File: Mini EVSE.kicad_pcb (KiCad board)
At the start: 2 copper layers, 49.5 x 76.8 mm, 46 parts, among them IC1 ATtiny84-20P, IC2 UCC23511QDWYRQ1, IC3 TLP3547_TP1,F_O, IC4 ISO224ADWV, J1 ICP, SW1 SW_DIP_x01, X1 15.36MHz

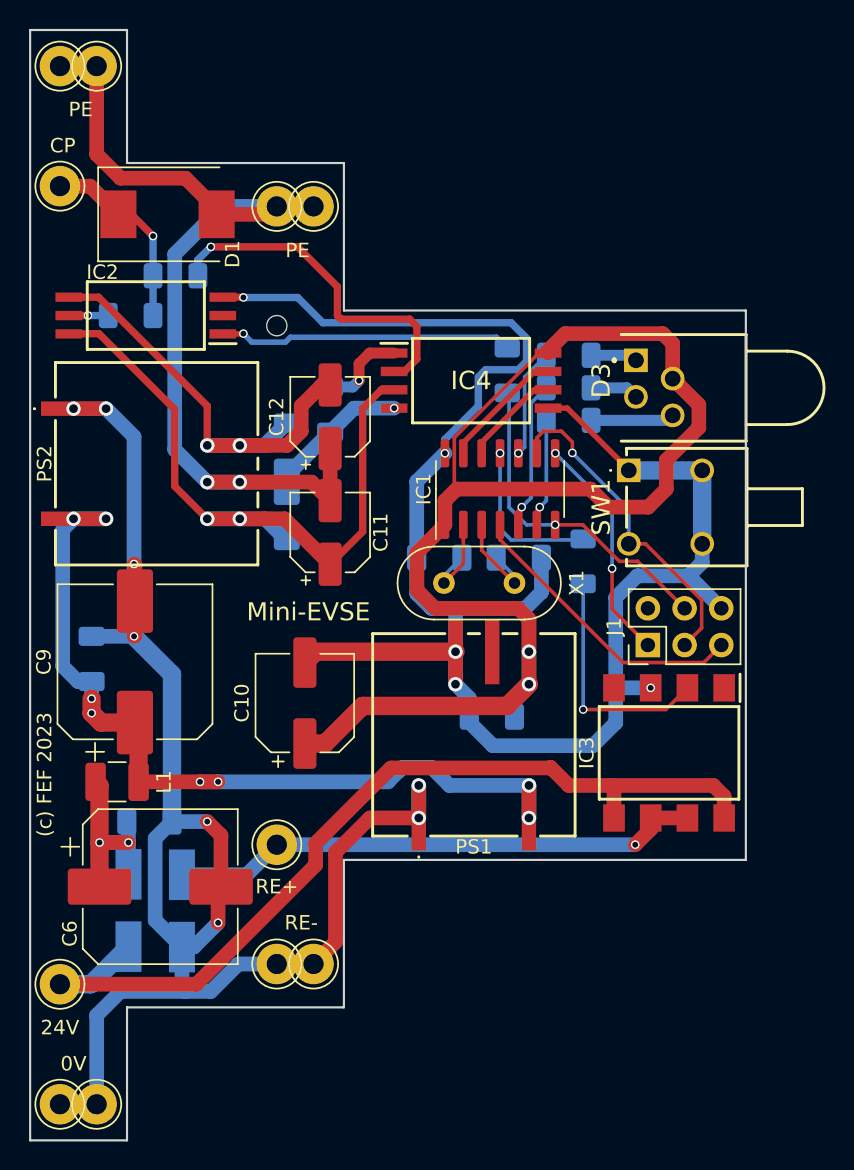
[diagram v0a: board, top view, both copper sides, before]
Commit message: More decoupling, layout adjustments
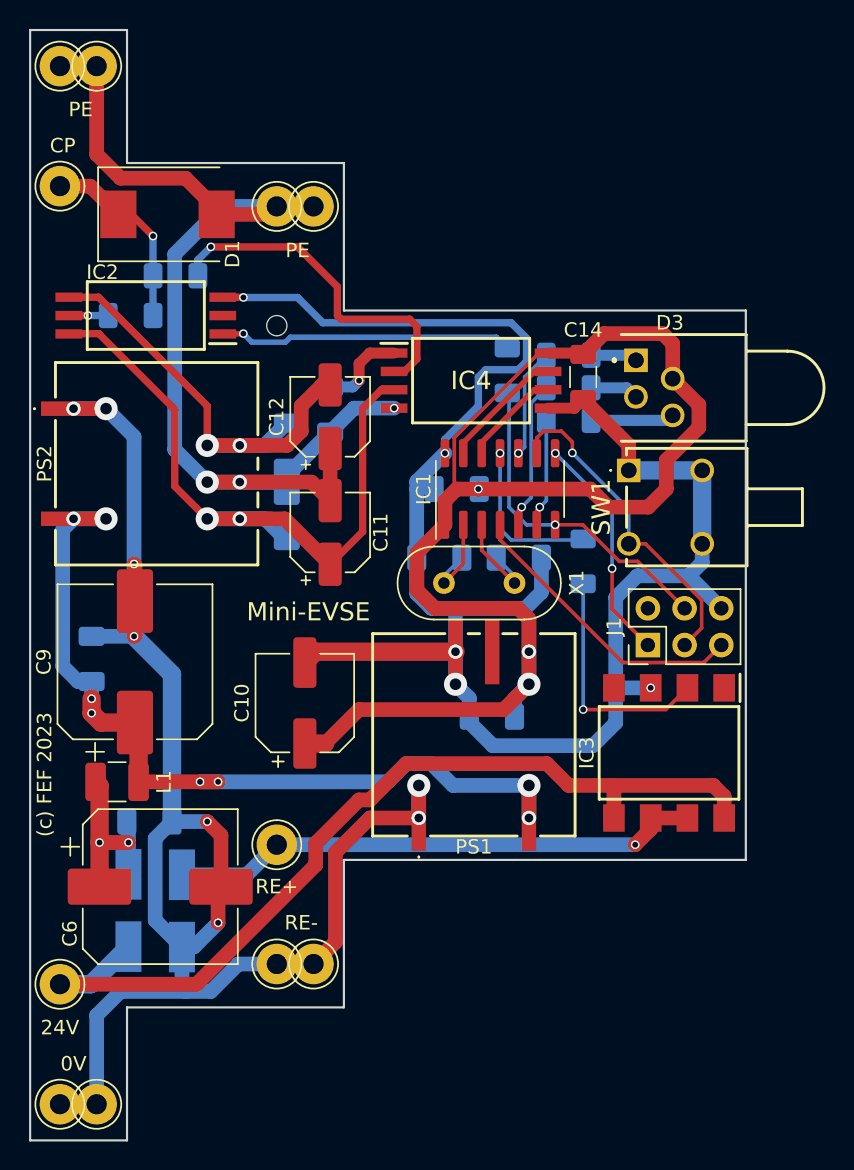
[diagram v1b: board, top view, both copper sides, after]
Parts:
- added C14: 10n, Capacitor_SMD:C_1206_3216Metric_Pad1.33x1.80mm_HandSolder, F.Cu at (138.2, 74.0)
- added C15: 10n, Capacitor_SMD:C_1206_3216Metric_Pad1.33x1.80mm_HandSolder, B.Cu at (129.5, 81.8)
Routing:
- net GND: track 126.8 -> 129.5 mm
- net +5V: track 90.4 -> 90.5 mm, vias 2 -> 3

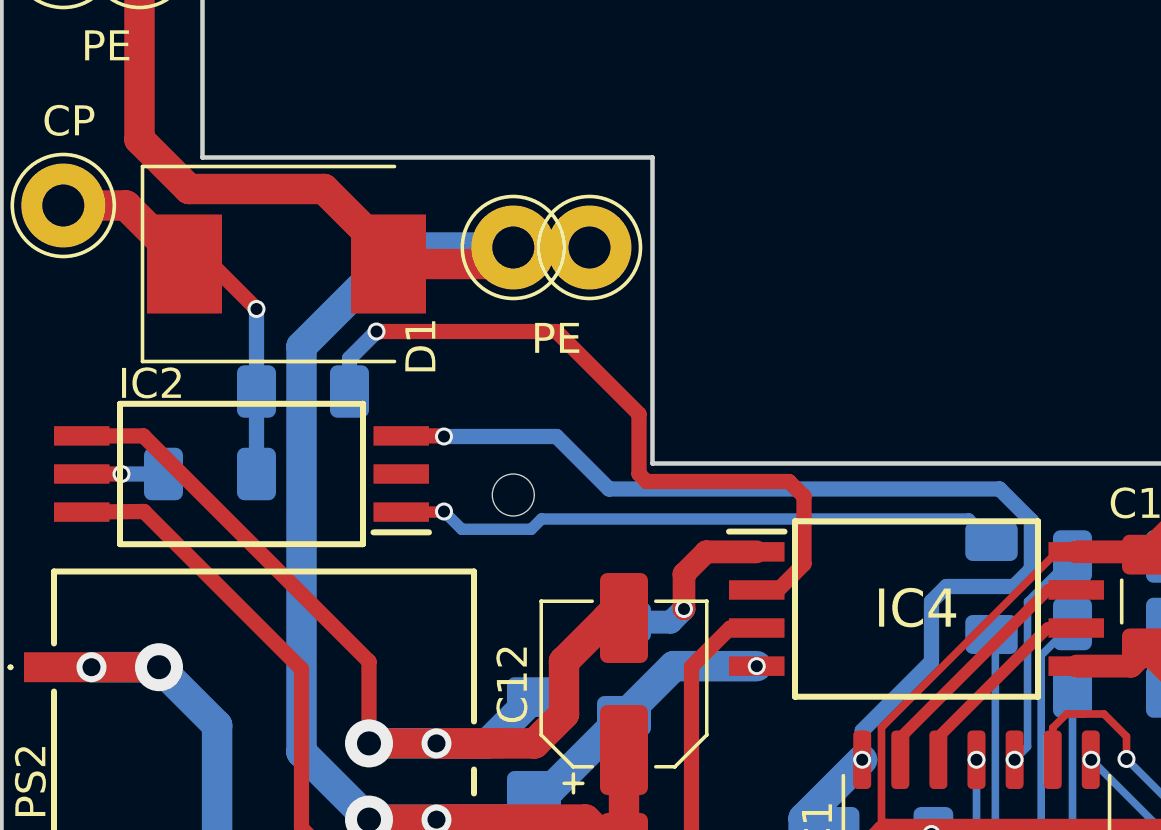
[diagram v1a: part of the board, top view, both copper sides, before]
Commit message: Added possible input decoupling cap
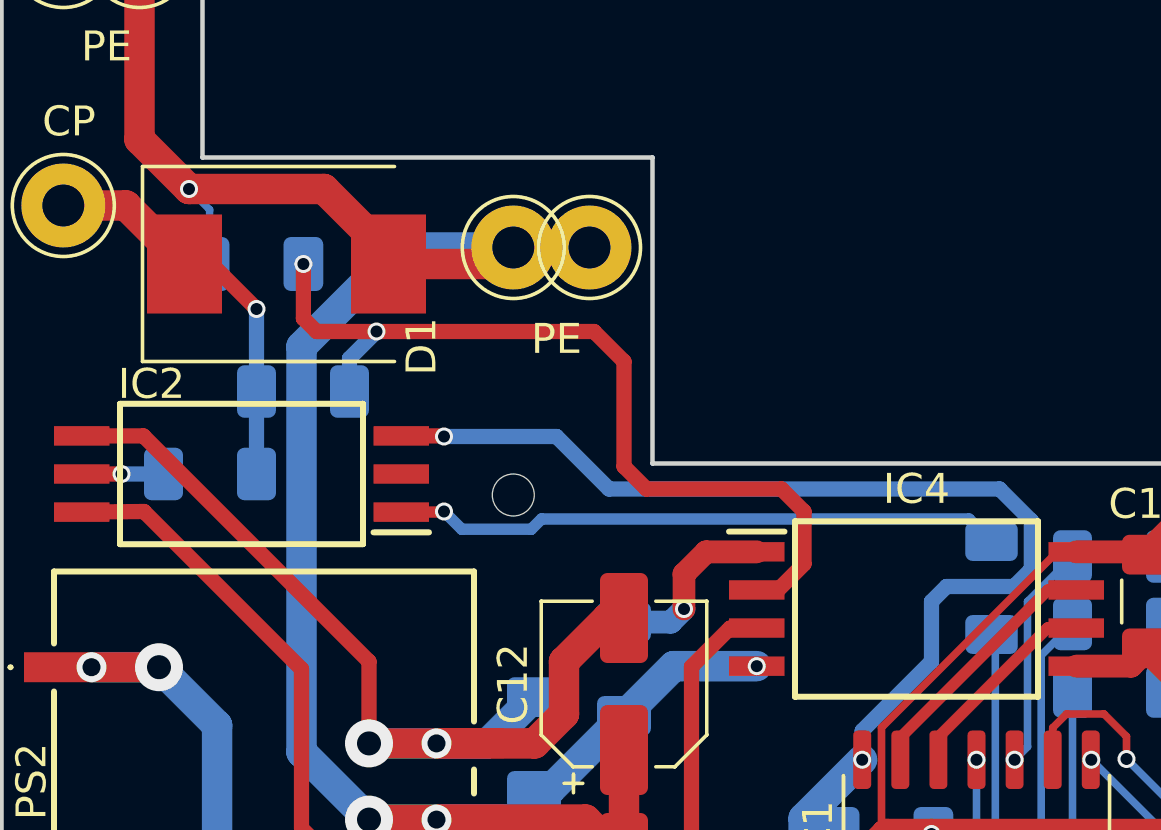
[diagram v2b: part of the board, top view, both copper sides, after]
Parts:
- added C16: 100p, Capacitor_SMD:C_1206_3216Metric_Pad1.33x1.80mm_HandSolder, B.Cu at (108.5, 62.8)
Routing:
- net Net-(IC4-Pad2): track 24.3 -> 29.3 mm, vias 1 -> 2
- net PE: track 77.8 -> 80.6 mm, vias 3 -> 4
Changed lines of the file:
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@@
     (property "Sheetname" "")
     (attr smd)
-    (fp_text reference "IC4" (at 0 0) (layer "F.SilkS")
-      (effects (font (size 1.27 1.27) (thickness 0.254)))
+    (fp_text reference "IC4" (at 0 -4) (layer "F.SilkS")
+      (effects (font (size 1 1) (thickness 0.15)))
     )
     (fp_text value "ISO224ADWV" (at 0 0) (layer "F.SilkS") hide
@@
       (net 32 "Net-(C13-Pad1)") (pintype "passive"))
     (pad "2" smd roundrect (at 1.5625 0 270) (size 1.325 1.8) (layers "B.Cu" "B.Paste" "B.Mask") (roundrect_rratio 0.188679)
+      (net 18 "PE") (pintype "passive"))
+    (model "${KICAD6_3DMODEL_DIR}/Capacitor_SMD.3dshapes/C_1206_3216Metric.wrl"
+      (offset (xyz 0 0 0))
+      (scale (xyz 1 1 1))
+      (rotate (xyz 0 0 0))
+    )
+  )
+  (footprint "Capacitor_SMD:C_1206_3216Metric_Pad1.33x1.80mm_HandSolder" (layer "B.Cu")
+    (at 108.5 62.75 180)
+    (descr "Capacitor SMD 1206 (3216 Metric), square (rectangular) end terminal, IPC_7351 nominal with elongated pad for handsoldering. (Body size source: IPC-SM-782 page 76, https://www.pcb-3d.com/wordpress/wp-content/uploads/ipc-sm-782a_amendment_1_and_2.pdf), generated with kicad-footprint-generator")
+    (tags "capacitor handsolder")
+    (property "Sheetfile" "Mini EVSE.kicad_sch")
+    (property "Sheetname" "")
+    (attr smd)
+    (fp_text reference "C16" (at 0 1.85) (layer "B.SilkS")
+      (effects (font (size 1 1) (thickness 0.15)) (justify mirror))
+    )
+    (fp_text value "100p" (at 0 -1.85) (layer "B.Fab")
+      (effects (font (size 1 1) (thickness 0.15)) (justify mirror))
+    )
+    (fp_text user "${REFERENCE}" (at 0 0) (layer "B.Fab")
+      (effects (font (size 0.8 0.8) (thickness 0.12)) (justify mirror))
+    )
+    (fp_line (start -0.711252 0.91) (end 0.711252 0.91) (layer "B.SilkS") (width 0.12))
+    (fp_line (start -0.711252 -0.91) (end 0.711252 -0.91) (layer "B.SilkS") (width 0.12))
+    (fp_line (start -2.48 1.15) (end 2.48 1.15) (layer "B.CrtYd") (width 0.05))
+    (fp_line (start 2.48 -1.15) (end -2.48 -1.15) (layer "B.CrtYd") (width 0.05))
+    (fp_line (start 2.48 1.15) (end 2.48 -1.15) (layer "B.CrtYd") (width 0.05))
+    (fp_line (start -2.48 -1.15) (end -2.48 1.15) (layer "B.CrtYd") (width 0.05))
+    (fp_line (start 1.6 0.8) (end 1.6 -0.8) (layer "B.Fab") (width 0.1))
+    (fp_line (start -1.6 0.8) (end 1.6 0.8) (layer "B.Fab") (width 0.1))
+    (fp_line (start -1.6 -0.8) (end -1.6 0.8) (layer "B.Fab") (width 0.1))
+    (fp_line (start 1.6 -0.8) (end -1.6 -0.8) (layer "B.Fab") (width 0.1))
+    (pad "1" smd roundrect (at -1.5625 0 180) (size 1.325 1.8) (layers "B.Cu" "B.Paste" "B.Mask") (roundrect_rratio 0.188679)
+      (net 35 "Net-(IC4-Pad2)") (pintype "passive"))
+    (pad "2" smd roundrect (at 1.5625 0 180) (size 1.325 1.8) (layers "B.Cu" "B.Paste" "B.Mask") (roundrect_rratio 0.188679)
       (net 18 "PE") (pintype "passive"))
     (model "${KICAD6_3DMODEL_DIR}/Capacitor_SMD.3dshapes/C_1206_3216Metric.wrl"
@@
   (segment (start 112.9 62.75) (end 116.51 62.75) (width 1.016) (layer "F.Cu") (net 18))
   (segment (start 119.47 81.27) (end 120.75 82.55) (width 1.016) (layer "F.Cu") (net 18))
+  (via (at 106.25 60.25) (size 0.6) (drill 0.4) (layers "F.Cu" "B.Cu") (net 18))
   (via (at 114.5 81.27) (size 1) (drill 0.6) (layers "F.Cu" "B.Cu") (net 18))
   (via (at 112.25 81.27) (size 1.6) (drill 0.8) (layers "F.Cu" "B.Cu") (free) (net 18))
   (via (at 125.175 76.155) (size 0.6) (drill 0.4) (layers "F.Cu" "B.Cu") (net 18))
+  (segment (start 106.9375 62.75) (end 106.9375 60.9375) (width 0.25) (layer "B.Cu") (net 18))
   (segment (start 117.75 81.25) (end 117.75 82.1875) (width 1.016) (layer "B.Cu") (net 18))
+  (segment (start 106.9375 60.9375) (end 106.25 60.25) (width 0.25) (layer "B.Cu") (net 18))
   (segment (start 125.175 76.155) (end 122.4075 76.155) (width 1.016) (layer "B.Cu") (net 18))
   (segment (start 117.75 80.3125) (end 117.75 81.25) (width 1.016) (layer "B.Cu") (net 18))
@@
   (segment (start 134.865 74.885) (end 135.825 74.885) (width 0.381) (layer "F.Cu") (net 34))
   (segment (start 131.23 79.275) (end 131.23 78.52) (width 0.381) (layer "F.Cu") (net 34))
-  (segment (start 126.75 70.5) (end 126.25 70) (width 0.508) (layer "F.Cu") (net 35))
-  (segment (start 121.25 69.75) (end 121.25 67.75) (width 0.508) (layer "F.Cu") (net 35))
-  (segment (start 118.5 65) (end 112.5 65) (width 0.508) (layer "F.Cu") (net 35))
-  (segment (start 121.5 70) (end 121.25 69.75) (width 0.508) (layer "F.Cu") (net 35))
-  (segment (start 126.25 70) (end 121.5 70) (width 0.508) (layer "F.Cu") (net 35))
+  (segment (start 120.75 66) (end 119.75 65) (width 0.508) (layer "F.Cu") (net 35))
+  (segment (start 126.75 72.75) (end 126.75 71) (width 0.508) (layer "F.Cu") (net 35))
+  (segment (start 121.5 70.25) (end 120.75 69.5) (width 0.508) (layer "F.Cu") (net 35))
+  (segment (start 126.75 71) (end 126 70.25) (width 0.508) (layer "F.Cu") (net 35))
+  (segment (start 126 70.25) (end 121.5 70.25) (width 0.508) (layer "F.Cu") (net 35))
+  (segment (start 125.175 73.615) (end 125.885 73.615) (width 0.508) (layer "F.Cu") (net 35))
+  (segment (start 112.5 65) (end 110.5 65) (width 0.508) (layer "F.Cu") (net 35))
+  (segment (start 119.75 65) (end 112.5 65) (width 0.508) (layer "F.Cu") (net 35))
+  (segment (start 120.75 69.5) (end 120.75 66) (width 0.508) (layer "F.Cu") (net 35))
+  (segment (start 110.5 65) (end 110.0625 64.5625) (width 0.508) (layer "F.Cu") (net 35))
+  (segment (start 110.0625 64.5625) (end 110.0625 62.75) (width 0.508) (layer "F.Cu") (net 35))
   (segment (start 125.885 73.615) (end 126.75 72.75) (width 0.508) (layer "F.Cu") (net 35))
-  (segment (start 126.75 72.75) (end 126.75 70.5) (width 0.508) (layer "F.Cu") (net 35))
-  (segment (start 125.175 73.615) (end 125.885 73.615) (width 0.508) (layer "F.Cu") (net 35))
-  (segment (start 121.25 67.75) (end 118.5 65) (width 0.508) (layer "F.Cu") (net 35))
   (via (at 112.5 65) (size 0.6) (drill 0.4) (layers "F.Cu" "B.Cu") (net 35))
+  (via (at 110.0625 62.75) (size 0.6) (drill 0.4) (layers "F.Cu" "B.Cu") (net 35))
   (segment (start 111.6 67) (end 111.6 65.9) (width 0.508) (layer "B.Cu") (net 35))
   (segment (start 111.6 65.9) (end 112.5 65) (width 0.508) (layer "B.Cu") (net 35))

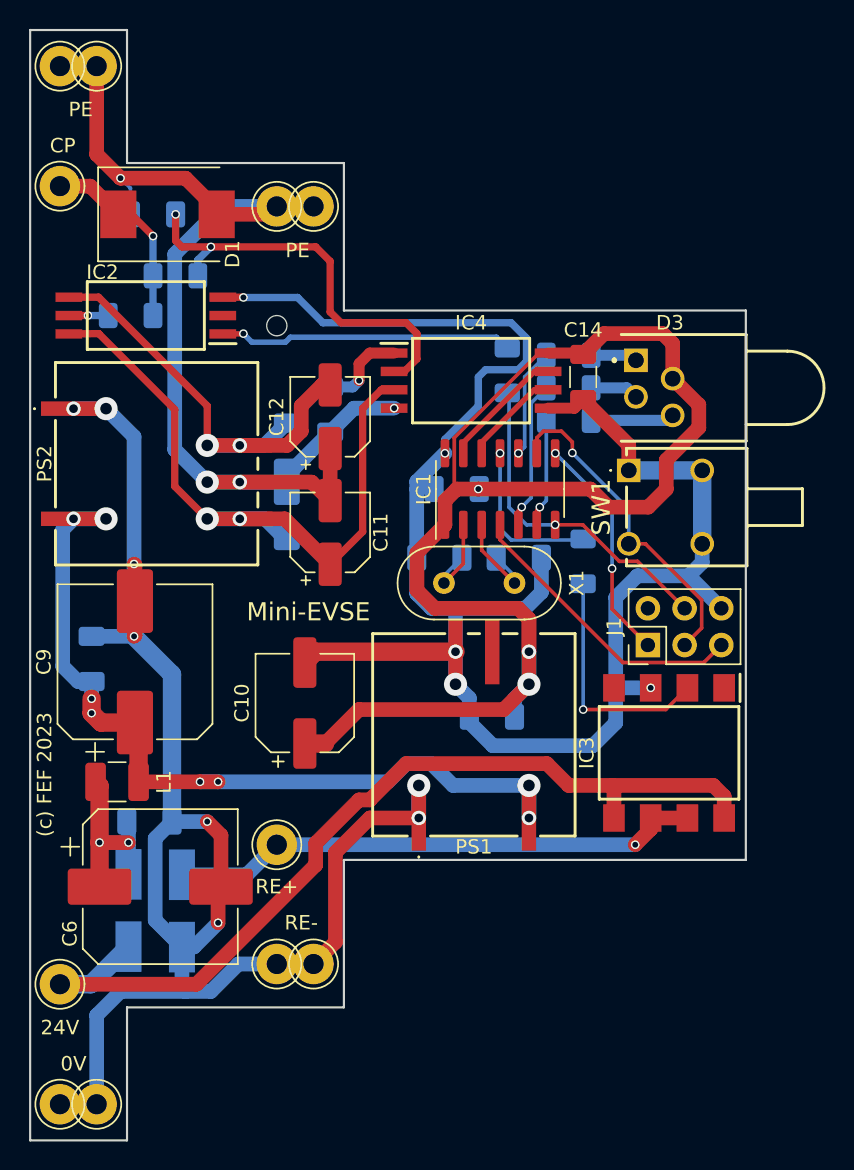
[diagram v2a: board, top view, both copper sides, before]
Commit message: Improved saftety distances
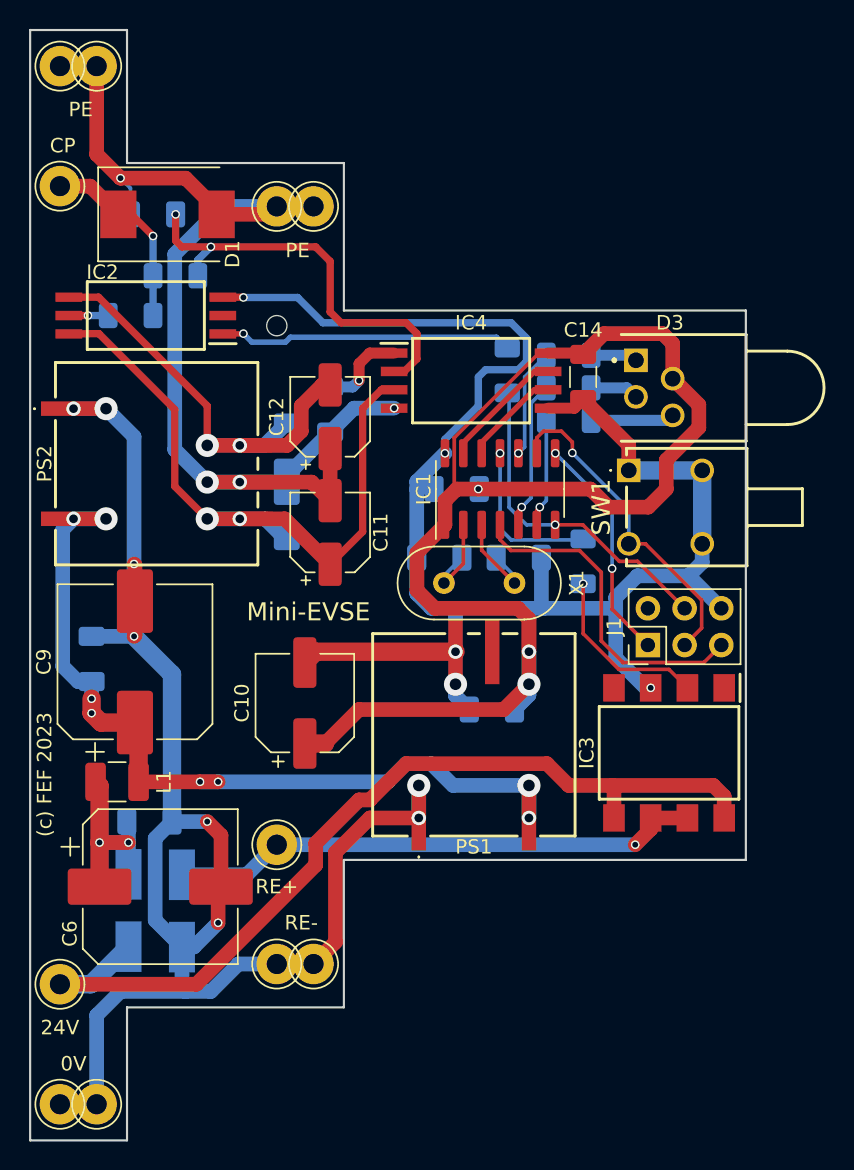
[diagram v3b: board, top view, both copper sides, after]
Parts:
- moved C2 0.50 mm to (131.9, 97.0)
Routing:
- net GND: track 129.5 -> 119.4 mm
- net Net-(IC3-Pad2): track 16.5 -> 12.2 mm
- net /RESET: track 20.4 -> 23.1 mm
- net +5V: track 90.5 -> 90.0 mm
